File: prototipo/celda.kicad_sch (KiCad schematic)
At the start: 13 parts, among them Q1 MMBT2222A, Q3 MMBT2907A, Q4 MMBT2222A

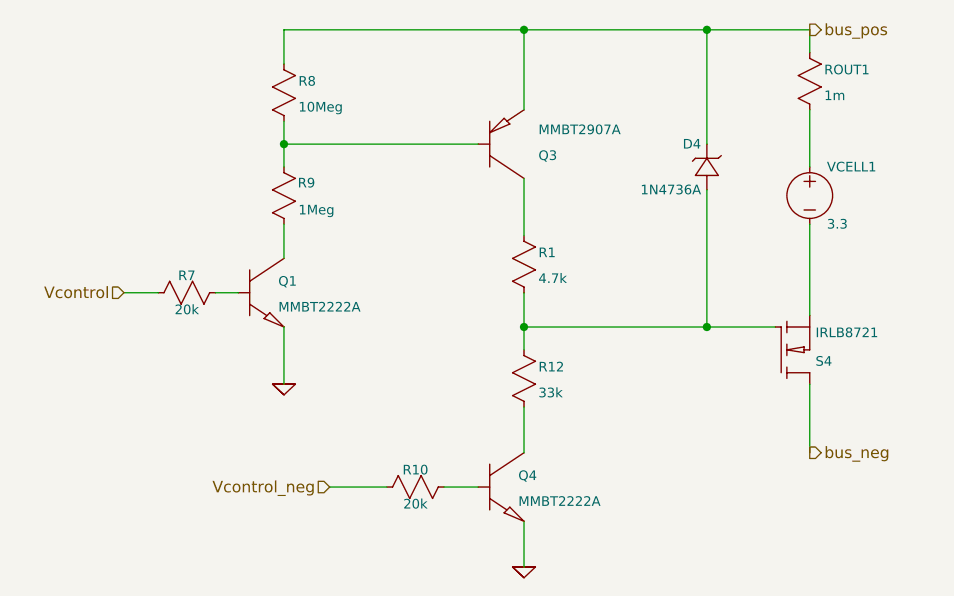
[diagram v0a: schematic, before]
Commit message: pruebo modulos de celdas en el esquematico del pcb
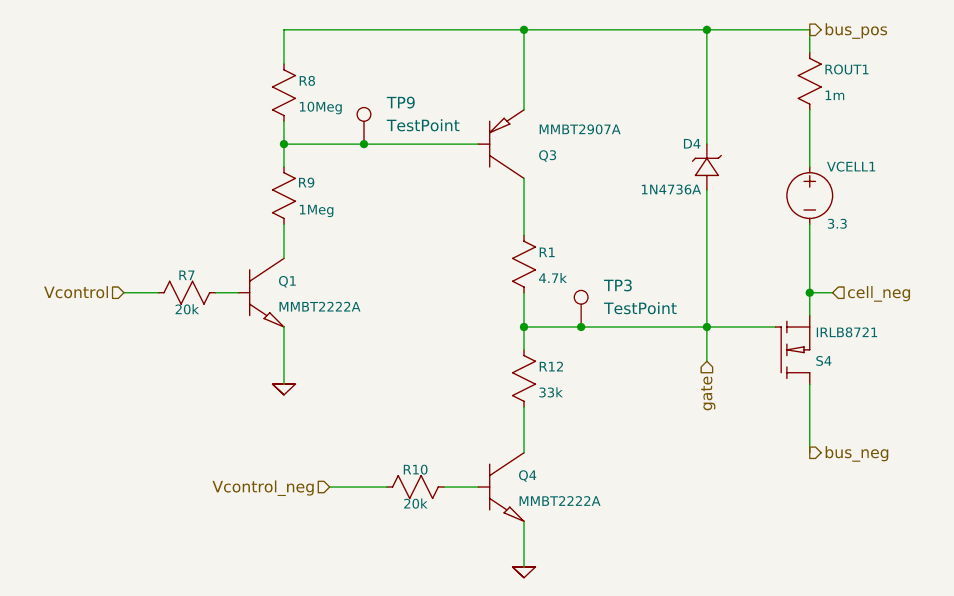
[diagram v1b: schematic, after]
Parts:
- added TP3, TP9: TestPoint, TestPoint:TestPoint_Bridge_Pitch2.54mm_Drill1.0mm, symbol Connector:TestPoint
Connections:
- net at Q3.1 (B), R8.2, R9.1: now also TP9.1
- net gate: now reaches D4.1 (+), R1.2, R12.1, S4.1 (G)
- net gate: now also TP3.1
- net cell_neg: now reaches S4.3 (S), VCELL1.2 (-)
